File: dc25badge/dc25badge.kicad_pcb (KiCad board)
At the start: 2 copper layers, 126.8 x 48.2 mm, 94 parts, among them P1 BATT, P2 USB_OTG, P3 CORTEX, SW1 RESET, SW3 MODE, SW4 BRIGHT, U1 MIC5305, U11 APA102, U12 APA102, U14 APA102, U15 APA102, U17 APA102, U18 APA102, U19 APA102, U2 TPS61232, U20 APA102, U21 APA102, U22 APA102, U23 APA102, U24 APA102, U25 APA102, U26 APA102, U27 APA102, U28 APA102, U29 APA102, U3 ATSAMD21E18A-AU, U30 APA102, U31 APA102, U32 APA102, U33 APA102, U34 APA102, U35 APA102, U36 APA102, U37 APA102, U38 APA102, U39 APA102, U4 74AHCT125, U40 APA102, U41 APA102, U42 APA102, U43 APA102, U44 APA102, U45 APA102, U46 APA102, U47 APA102, U48 APA102, U49 APA102, U50 APA102, U51 APA102, U52 APA102, U53 APA102, U54 APA102, U55 APA102, U56 APA102, U57 APA102, U58 APA102, U61 APA102, U64 APA102, Y1 32.768k

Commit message: Remove use of CS line.
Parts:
- removed R7: 10k, Resistors_SMD:R_0805_HandSoldering
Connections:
- net SOFT_PWR renamed Net-(U3-Pad6)
- U3 pad 19: SPI_EN -> Net-(U3-Pad19)
- U4 pad 1: SPI_EN -> GND
- U4 pad 4: SPI_EN -> GND
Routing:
- net SPI_EN: track 23.6 -> 0.00 mm
- net +3V3: track 65.0 -> 62.1 mm

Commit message: Add some noise isolation around SPI lines.
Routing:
- net GND: track 204.6 -> 240.9 mm, vias 49 -> 51
- net SPI_CLK: track 27.1 -> 22.8 mm
- net MOSI3: track 19.2 -> 15.1 mm

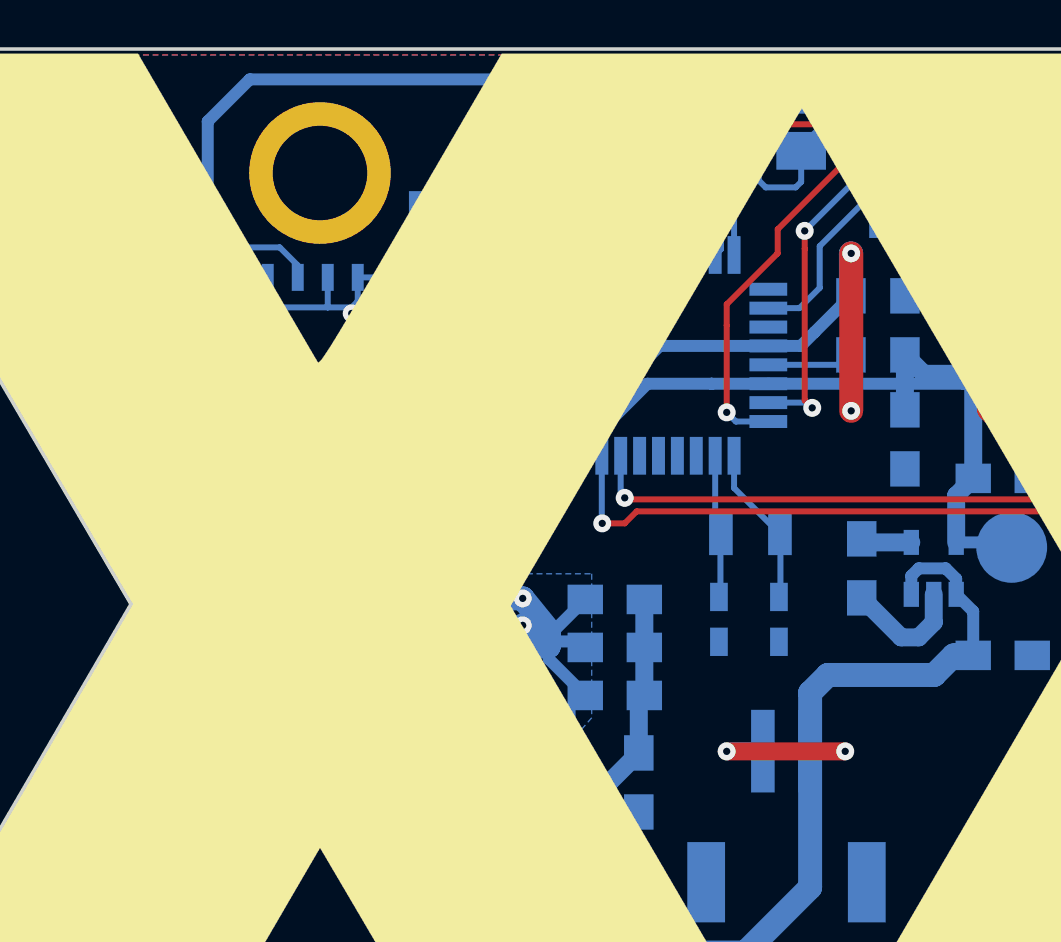
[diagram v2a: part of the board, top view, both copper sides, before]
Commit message: Add indicator LED.
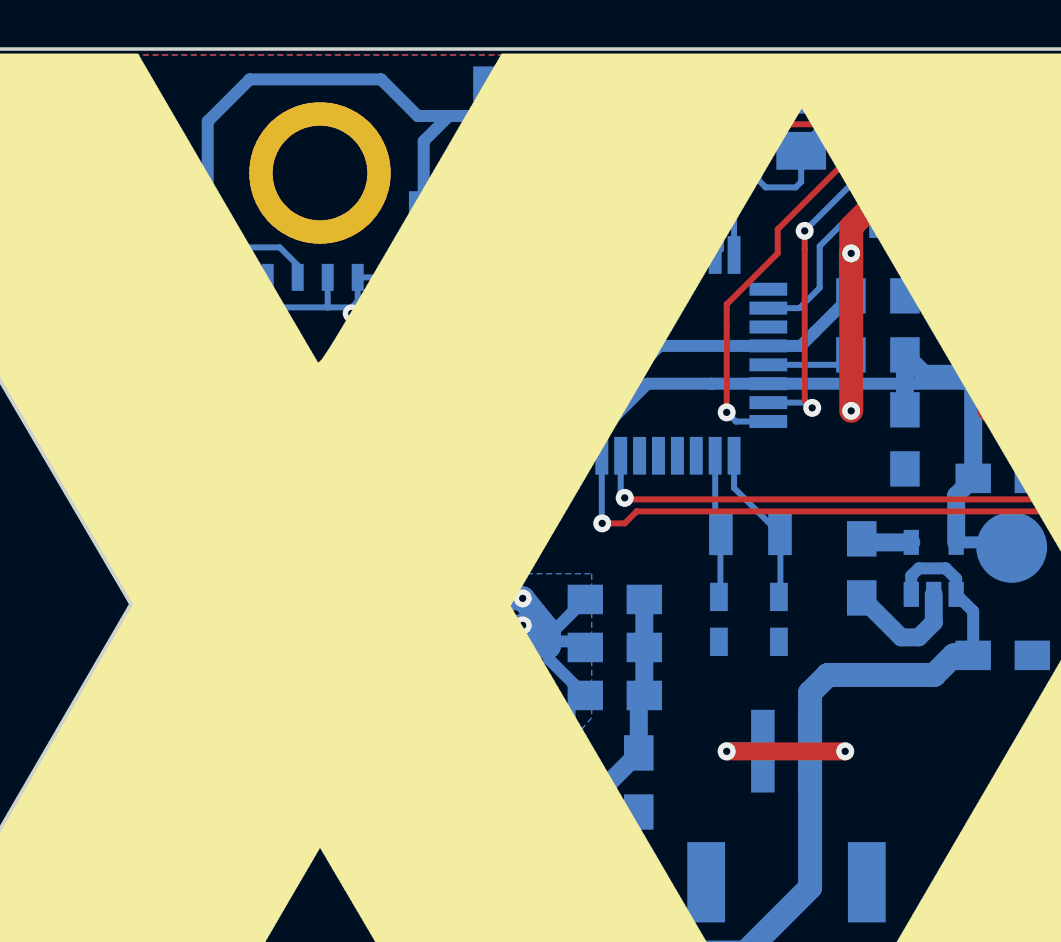
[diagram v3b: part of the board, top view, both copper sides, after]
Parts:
- added D1: LED, LEDs:LED_0805, B.Cu at (61.7, 35.3)
- added R1: 1k, Resistors_SMD:R_0805_HandSoldering, B.Cu at (59.4, 35.6)
- moved C7 2.60 mm to (60.4, 50.6), turned to 270 degrees
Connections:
- REF** pad : (no net) -> GND (x2)
- U3 pad 18: Net-(U3-Pad18) -> SCLK3
- U3 pad 19: Net-(U3-Pad19) -> LED_GLOBAL
- U3 pad 20: SCLK3 -> Net-(U3-Pad20)
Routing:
- net GND: track 240.9 -> 257.9 mm, vias 51 -> 52
- net LED_GLOBAL: track 0.00 -> 8.90 mm
- net Net-(D1-Pad2): track 0.00 -> 2.35 mm
- net SCLK3: track 24.1 -> 21.8 mm

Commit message: PCB with LED.
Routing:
- net +5V: track 95.0 -> 108.8 mm, vias 16 -> 19
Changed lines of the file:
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@@
     (links 303)
     (no_connects 0)
-    (area 30.924999 32.674999 157.825001 81.075001)
+    (area 15.150001 25.3 158.498136 83.1882)
     (thickness 1.6)
     (drawings 14)
-    (tracks 1069)
+    (tracks 1078)
     (zones 0)
     (modules 95)
@@
   (page A4)
   (layers
-    (0 F.Cu signal hide)
-    (31 B.Cu signal hide)
+    (0 F.Cu signal)
+    (31 B.Cu signal)
     (32 B.Adhes user)
     (33 F.Adhes user)
@@
   )
   (setup
-    (last_trace_width 0.508)
+    (last_trace_width 1.016)
     (user_trace_width 0.254)
     (user_trace_width 0.508)
@@
   (segment (start 79.184 53.637) (end 79.184 51.648) (width 0.762) (layer B.Cu) (net 3) (status 10))
   (segment (start 79.184 51.648) (end 79.905 50.927) (width 0.762) (layer B.Cu) (net 3) (status 20))
+  (segment (start 101.1335 69.9865) (end 99.1521 69.9865) (width 1.016) (layer F.Cu) (net 4) (status 400000))
+  (via (at 103.886 67.7926) (size 0.762) (drill 0.3048) (layers F.Cu B.Cu) (net 4))
+  (segment (start 101.346 67.7926) (end 103.886 67.7926) (width 1.016) (layer B.Cu) (net 4))
+  (segment (start 99.1108 70.0278) (end 101.346 67.7926) (width 1.016) (layer B.Cu) (net 4))
+  (via (at 99.1108 70.0278) (size 0.762) (drill 0.3048) (layers F.Cu B.Cu) (net 4))
+  (segment (start 99.1521 69.9865) (end 99.1108 70.0278) (width 1.016) (layer F.Cu) (net 4))
+  (segment (start 102.6795 76.073) (end 105.3338 76.073) (width 1.016) (layer B.Cu) (net 4))
+  (via (at 107.7214 73.6854) (size 0.762) (drill 0.3048) (layers F.Cu B.Cu) (net 4))
+  (segment (start 105.3338 76.073) (end 107.7214 73.6854) (width 1.016) (layer B.Cu) (net 4))
   (segment (start 105.4735 55.4355) (end 102.1965 55.4355) (width 0.508) (layer B.Cu) (net 4))
   (segment (start 102.1965 55.4355) (end 101.986 55.646) (width 0.508) (layer B.Cu) (net 4))

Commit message: Migrate schematic/PCB changes.
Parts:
- removed W1: GND, Measurement_Points:Measurement_Point_Round-SMD-Pad_Big
- added Q1: DMN1019USN, TO_SOT_Packages_SMD:SOT-23, B.Cu at (71.0, 73.2)
- C1, C10, C11, C14, C15, C16, C18, C19, C2, C20, C21, C22, C24, C25, C26, C27, C3, C4, C5, C6, C7, C8, C9: footprint Capacitors_SMD:C_0805_HandSoldering -> Capacitors_SMD:C_0805
- C12, C13: footprint Capacitors_SMD:C_0603_HandSoldering -> Capacitors_SMD:C_0603
- R1: value 1k -> 330; footprint Resistors_SMD:R_0805_HandSoldering -> Resistors_SMD:R_0805
- R5, R6: footprint Resistors_SMD:R_0805_HandSoldering -> Resistors_SMD:R_0805
- moved R1 2.54 mm to (59.8, 38.1)
- moved D1 0.95 mm to (60.8, 35.4), turned to 180 degrees
- moved P1 0.79 mm to (72.0, 66.0)
- moved C4 0.43 mm to (61.3, 68.2)
- moved C7 0.18 mm to (60.4, 50.4)
- moved C12 0.13 mm to (69.2, 56.8)
- moved C13 0.13 mm to (71.7, 56.8)
- moved C10 0.06 mm to (77.0, 49.2)
- moved C9 0.06 mm to (74.7, 44.5)
- moved C11 0.06 mm to (77.0, 44.5)
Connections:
- P1 pad : (no net) -> GND
- P1 pad 2: GND -> Net-(P1-Pad2)
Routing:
- net /VBAT: track 49.8 -> 65.0 mm
- net Net-(P1-Pad2): track 0.00 -> 8.89 mm
- net GND: track 257.9 -> 256.1 mm, vias 52 -> 50
- net LED_GLOBAL: track 8.90 -> 7.65 mm
- net ~RESET: track 35.9 -> 36.5 mm
- net Net-(D1-Pad2): track 2.35 -> 1.79 mm

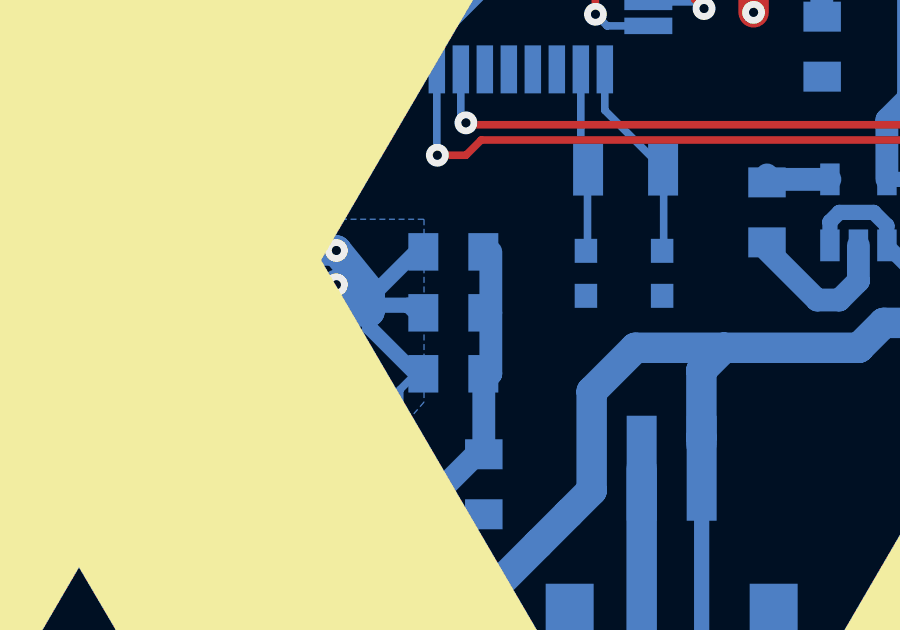
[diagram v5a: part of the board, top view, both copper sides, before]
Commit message: More cap for noise.
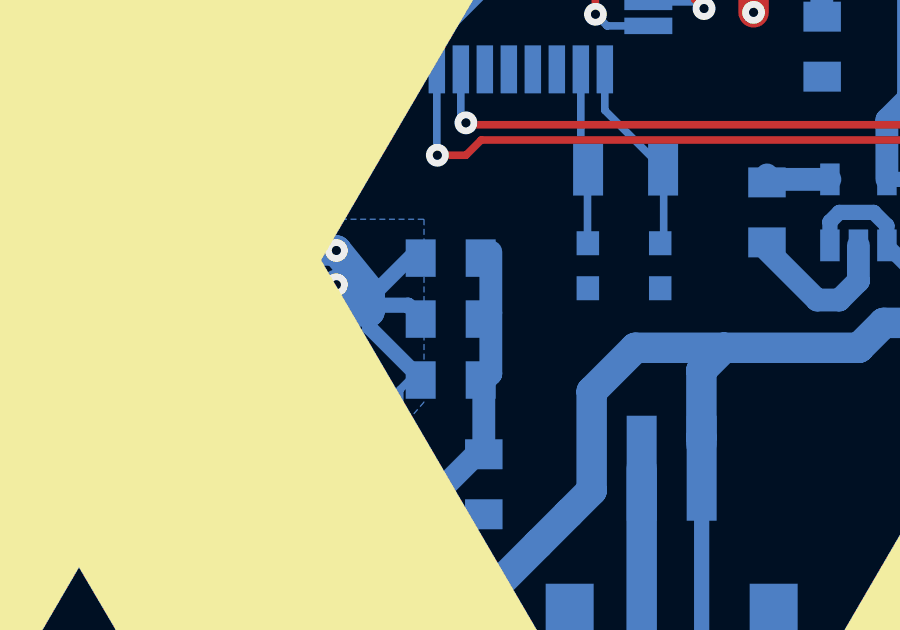
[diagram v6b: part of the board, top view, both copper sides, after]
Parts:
- added C17: 1u, Capacitors_SMD:C_0805, B.Cu at (58.7, 58.0)
- moved C12 0.26 mm to (69.2, 56.5)
- moved C13 0.26 mm to (71.6, 56.5)
- moved C27 0.23 mm to (64.6, 60.3)
- moved C6 0.23 mm to (64.6, 56.3)
- moved C14 0.23 mm to (64.6, 58.3)
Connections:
- P1 pad : GND -> (no net)
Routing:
- net +5V: track 108.8 -> 110.0 mm
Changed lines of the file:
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@@
     (thickness 1.6)
     (drawings 14)
-    (tracks 1095)
+    (tracks 1097)
     (zones 0)
-    (modules 95)
+    (modules 96)
     (nets 147)
   )
@@
   )
   (setup
-    (last_trace_width 1.016)
+    (last_trace_width 0.254)
     (user_trace_width 0.254)
     (user_trace_width 0.508)
@@
     (pad 2 smd rect (at 1 2.775 180) (size 1 3.5) (layers B.Cu B.Paste B.Mask)
       (net 146 "Net-(P1-Pad2)"))
-    (pad "" smd rect (at -3.4 -2.775 180) (size 1.6 3.4) (layers B.Cu B.Paste B.Mask)
-      (net 1 GND))
-    (pad "" smd rect (at 3.4 -2.775 180) (size 1.6 3.4) (layers B.Cu B.Paste B.Mask)
-      (net 1 GND))
+    (pad "" smd rect (at -3.4 -2.775 180) (size 1.6 3.4) (layers B.Cu B.Paste B.Mask))
+    (pad "" smd rect (at 3.4 -2.775 180) (size 1.6 3.4) (layers B.Cu B.Paste B.Mask))
   )
   (module TO_SOT_Packages_SMD:SOT-23-5 (layer B.Cu)
@@
   )
   (module Capacitors_SMD:C_0603 (layer B.Cu)
-    (at 69.1515 56.769 270)
+    (at 69.215 56.515 270)
     (descr "Capacitor SMD 0603, reflow soldering, AVX (see smccp.pdf)")
     (tags "capacitor 0603")
@@
   )
   (module Capacitors_SMD:C_0603 (layer B.Cu)
-    (at 71.6915 56.769 270)
+    (at 71.628 56.515 270)
     (descr "Capacitor SMD 0603, reflow soldering, AVX (see smccp.pdf)")
     (tags "capacitor 0603")
@@
   )
   (module Capacitors_SMD:C_0805 (layer B.Cu)
-    (at 64.731 56.053)
+    (at 64.643 56.261)
     (descr "Capacitor SMD 0805, reflow soldering, AVX (see smccp.pdf)")
     (tags "capacitor 0805")
@@
   )
   (module Capacitors_SMD:C_0805 (layer B.Cu)
-    (at 64.731 58.085)
+    (at 64.643 58.293)
     (descr "Capacitor SMD 0805, reflow soldering, AVX (see smccp.pdf)")
     (tags "capacitor 0805")
@@
   )
   (module Capacitors_SMD:C_0805 (layer B.Cu)
-    (at 64.731 60.117)
+    (at 64.643 60.325)
     (descr "Capacitor SMD 0805, reflow soldering, AVX (see smccp.pdf)")
     (tags "capacitor 0805")
@@
     )
   )
+  (module Capacitors_SMD:C_0805 (layer B.Cu)
+    (at 58.674 58.039 180)
+    (descr "Capacitor SMD 0805, reflow soldering, AVX (see smccp.pdf)")
+    (tags "capacitor 0805")
+    (attr smd)
+    (fp_text reference C17 (at 0 1.651 180) (layer B.SilkS)
+      (effects (font (size 0.8 0.8) (thickness 0.15)) (justify mirror))
+    )
+    (fp_text value 1u (at 0 -2.1 180) (layer B.Fab)
+      (effects (font (size 1 1) (thickness 0.15)) (justify mirror))
+    )
+    (fp_line (start -1 -0.625) (end -1 0.625) (layer B.Fab) (width 0.15))
+    (fp_line (start 1 -0.625) (end -1 -0.625) (layer B.Fab) (width 0.15))
+    (fp_line (start 1 0.625) (end 1 -0.625) (layer B.Fab) (width 0.15))
+    (fp_line (start -1 0.625) (end 1 0.625) (layer B.Fab) (width 0.15))
+    (fp_line (start -1.8 1) (end 1.8 1) (layer B.CrtYd) (width 0.05))
+    (fp_line (start -1.8 -1) (end 1.8 -1) (layer B.CrtYd) (width 0.05))
+    (fp_line (start -1.8 1) (end -1.8 -1) (layer B.CrtYd) (width 0.05))
+    (fp_line (start 1.8 1) (end 1.8 -1) (layer B.CrtYd) (width 0.05))
+    (fp_line (start 0.5 0.85) (end -0.5 0.85) (layer B.SilkS) (width 0.15))
+    (fp_line (start -0.5 -0.85) (end 0.5 -0.85) (layer B.SilkS) (width 0.15))
+    (pad 1 smd rect (at -1 0 180) (size 1 1.25) (layers B.Cu B.Paste B.Mask)
+      (net 4 +5V))
+    (pad 2 smd rect (at 1 0 180) (size 1 1.25) (layers B.Cu B.Paste B.Mask)
+      (net 1 GND))
+    (model Capacitors_SMD.3dshapes/C_0805.wrl
+      (at (xyz 0 0 0))
+      (scale (xyz 1 1 1))
+      (rotate (xyz 0 0 0))
+    )
+  )
   (dimension 48 (width 0.3) (layer Dwgs.User)
     (gr_text "48.000 mm" (at 21.65 57 90) (layer Dwgs.User)
@@
   (segment (start 79.184 53.637) (end 79.184 51.648) (width 0.762) (layer B.Cu) (net 3) (status 10))
   (segment (start 79.184 51.648) (end 79.905 50.927) (width 0.762) (layer B.Cu) (net 3) (status 20))
+  (segment (start 59.674 58.039) (end 60.579 58.039) (width 0.254) (layer B.Cu) (net 4))
+  (segment (start 61.087 58.039) (end 60.833 58.293) (width 1.016) (layer B.Cu) (net 4))
+  (via (at 60.833 58.293) (size 0.762) (drill 0.3048) (layers F.Cu B.Cu) (net 4))
+  (segment (start 61.087 58.039) (end 61.937 58.039) (width 1.016) (layer B.Cu) (net 4))
+  (segment (start 60.579 58.039) (end 60.833 58.293) (width 0.254) (layer B.Cu) (net 4))
   (segment (start 101.1335 69.9865) (end 99.1521 69.9865) (width 1.016) (layer F.Cu) (net 4))
   (via (at 103.886 67.7926) (size 0.762) (drill 0.3048) (layers F.Cu B.Cu) (net 4))
@@
   (segment (start 61.214 57.531) (end 60.833 57.15) (width 1.016) (layer B.Cu) (net 4))
   (segment (start 61.937 58.039) (end 61.937 57.531) (width 1.016) (layer B.Cu) (net 4))
-  (segment (start 61.937 58.039) (end 61.087 58.039) (width 1.016) (layer B.Cu) (net 4))
-  (via (at 60.833 58.293) (size 0.762) (drill 0.3048) (layers F.Cu B.Cu) (net 4))
-  (segment (start 61.087 58.039) (end 60.833 58.293) (width 1.016) (layer B.Cu) (net 4))
   (segment (start 53.594 43.688) (end 53.594 43.942) (width 0.254) (layer B.Cu) (net 4))
   (via (at 53.594 43.942) (size 0.762) (drill 0.3048) (layers F.Cu B.Cu) (net 4))
@@
   (segment (start 69.342 64.008) (end 69.342 60.706) (width 1.016) (layer B.Cu) (net 128))
   (segment (start 68.58 64.77) (end 69.342 64.008) (width 1.016) (layer B.Cu) (net 128))
-  (segment (start 71.943 74.152) (end 72.406 74.152) (width 0.508) (layer B.Cu) (net 128) (status 400000))
-  (segment (start 73.009 73.549) (end 73.009 63.265) (width 0.508) (layer B.Cu) (net 128) (status 800000))
+  (segment (start 71.943 74.152) (end 72.406 74.152) (width 0.508) (layer B.Cu) (net 128))
+  (segment (start 73.009 73.549) (end 73.009 63.265) (width 0.508) (layer B.Cu) (net 128))
   (segment (start 72.406 74.152) (end 73.009 73.549) (width 0.508) (layer B.Cu) (net 128))
   (segment (start 62.341 68.199) (end 62.341 67.994) (width 1.016) (layer B.Cu) (net 128))
@@
   (segment (start 59.7535 37.15) (end 59.7535 35.40252) (width 0.254) (layer B.Cu) (net 145))
   (segment (start 59.7535 35.40252) (end 59.72048 35.3695) (width 0.254) (layer B.Cu) (net 145))
-  (segment (start 71.009 63.265) (end 71.009 72.136) (width 1.016) (layer B.Cu) (net 146) (status C00000))
-  (segment (start 71.009 72.136) (end 70.993 72.152) (width 1.016) (layer B.Cu) (net 146) (status C00000))
+  (segment (start 71.009 63.265) (end 71.009 72.136) (width 1.016) (layer B.Cu) (net 146))
+  (segment (start 71.009 72.136) (end 70.993 72.152) (width 1.016) (layer B.Cu) (net 146))
   (zone (net 128) (net_name /VBAT) (layer B.Cu) (hatch full 0.508)
     (priority 5)

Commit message: Add option for anti-ringing resistors.
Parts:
- added R2: 330, Resistors_SMD:R_0805, B.Cu at (43.6, 46.5)
- added R3: 330, Resistors_SMD:R_0805, B.Cu at (47.1, 52.1)
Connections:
- U4 pad 3: SPI_MOSI -> Net-(R3-Pad1)
- U4 pad 6: SPI_CLK -> Net-(R2-Pad1)
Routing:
- net SPI_MOSI: track 31.6 -> 24.9 mm
- net SPI_CLK: track 22.8 -> 16.6 mm
- net Net-(R3-Pad1): track 0.00 -> 5.35 mm
- net Net-(R2-Pad1): track 0.00 -> 5.16 mm

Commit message: Update board.
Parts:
- added C23: NP, Capacitors_SMD:C_0805, B.Cu at (108.7, 56.8)
- added C28: NP, Capacitors_SMD:C_0805, B.Cu at (78.0, 62.1)
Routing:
- net GND: track 256.1 -> 279.2 mm
- net +5V: track 110.0 -> 113.4 mm
- net /VBAT: track 65.0 -> 67.0 mm
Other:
- board text added: "+"
- board text added: "Designed By @Matir"
- board text added: "Hack All The Things!"
